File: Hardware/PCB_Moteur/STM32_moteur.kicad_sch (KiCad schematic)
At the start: 37 parts, among them J7 Conn_01x06_Pin, U5 STM32F103CBT6, Y1 830050510

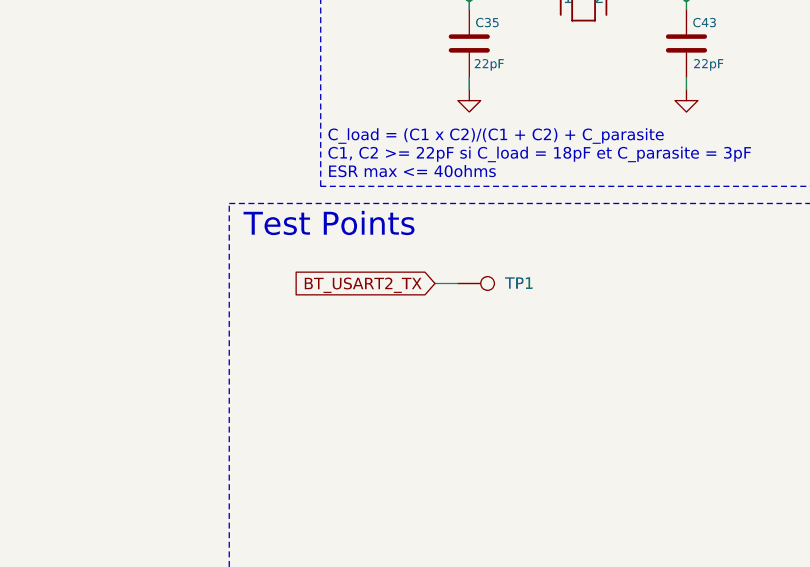
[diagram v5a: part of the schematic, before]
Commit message: fix(moteur + gse): move xt30 to border + fix silkscreen + connect shield to gnd  in pressure sensor + remake rounded corners + fix/add doc
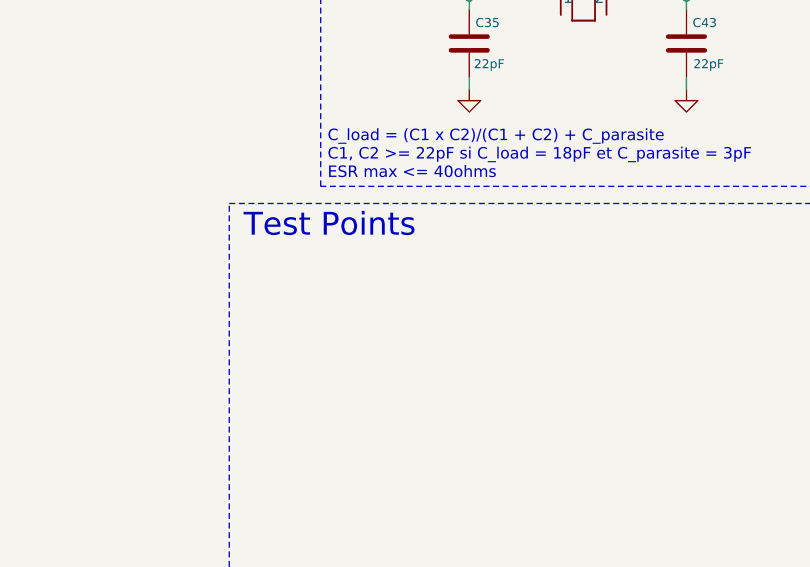
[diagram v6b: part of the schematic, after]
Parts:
- removed TP1: TestPoint, TestPoint:TestPoint_Pad_D1.0mm, symbol Connector:TestPoint
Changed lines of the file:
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@@
 	(wire
 		(pts
-			(xy 241.3 128.27) (xy 238.76 128.27)
+			(xy 242.57 105.41) (xy 242.57 106.68)
 		)
 		(stroke
@@
 	(wire
 		(pts
-			(xy 242.57 105.41) (xy 242.57 106.68)
+			(xy 146.05 44.45) (xy 146.05 46.99)
 		)
 		(stroke
@@
 	(wire
 		(pts
-			(xy 146.05 44.45) (xy 146.05 46.99)
+			(xy 215.9 25.4) (xy 218.44 25.4)
 		)
 		(stroke
@@
 	(wire
 		(pts
-			(xy 215.9 25.4) (xy 218.44 25.4)
+			(xy 148.59 127) (xy 151.13 127)
 		)
 		(stroke
@@
 	(wire
 		(pts
-			(xy 148.59 127) (xy 151.13 127)
+			(xy 132.08 82.55) (xy 133.35 82.55)
 		)
 		(stroke
@@
 	(wire
 		(pts
-			(xy 132.08 82.55) (xy 133.35 82.55)
+			(xy 166.37 67.31) (xy 173.99 67.31)
 		)
 		(stroke
@@
 	(wire
 		(pts
-			(xy 166.37 67.31) (xy 173.99 67.31)
+			(xy 132.08 102.87) (xy 133.35 102.87)
 		)
 		(stroke
@@
 		)
 	)
-	(wire
-		(pts
-			(xy 132.08 102.87) (xy 133.35 102.87)
-		)
-		(stroke
-			(width 0)
-			(type default)
-		)
-	)
 	(global_label "SYS_SWDIO"
 		(shape input)
@@
 				)
 				(justify left)
-				(hide yes)
-			)
-		)
-	)
-	(global_label "BT_USART2_TX"
-		(shape input)
-		(at 238.76 128.27 180)
-		(fields_autoplaced yes)
-		(effects
-			(font
-				(size 1.27 1.27)
-			)
-			(justify right)
-		)
-		(property "Intersheetrefs" "${INTERSHEET_REFS}"
-			(at 222.3492 128.27 0)
-			(effects
-				(font
-					(size 1.27 1.27)
-				)
-				(justify right)
 				(hide yes)
 			)
@@
 					(unit 1)
 				)
-			)
-		)
-	)
-	(symbol
-		(lib_id "Connector:TestPoint")
-		(at 241.3 128.27 270)
-		(mirror x)
-		(unit 1)
-		(exclude_from_sim no)
-		(in_bom yes)
-		(on_board yes)
-		(dnp no)
-		(property "Reference" "TP1"
-			(at 248.158 128.27 90)
-			(effects
-				(font
-					(size 1.27 1.27)
-				)
-			)
-		)
-		(property "Value" "TestPoint"
-			(at 244.602 125.73 90)
-			(effects
-				(font
-					(size 1.27 1.27)
-				)
-				(hide yes)
-			)
-		)
-		(property "Footprint" "TestPoint:TestPoint_Pad_D1.0mm"
-			(at 241.3 123.19 0)
-			(effects
-				(font
-					(size 1.27 1.27)
-				)
-				(hide yes)
-			)
-		)
-		(property "Datasheet" "-"
-			(at 241.3 123.19 0)
-			(effects
-				(font
-					(size 1.27 1.27)
-				)
-				(hide yes)
-			)
-		)
-		(property "Description" "test point"
-			(at 241.3 128.27 0)
-			(effects
-				(font
-					(size 1.27 1.27)
-				)
-				(hide yes)
-			)
-		)
-		(property "DigiKey_Part_Number" "-"
-			(at 241.3 128.27 90)
-			(effects
-				(font
-					(size 1.27 1.27)
-				)
-				(hide yes)
-			)
-		)
-		(property "Manufacturer_Part_Number" "-"
-			(at 241.3 128.27 90)
-			(effects
-				(font
-					(size 1.27 1.27)
-				)
-				(hide yes)
-			)
-		)
-		(pin "1"
-		)
-		(instances
-			(project "PCB_moteur"
-				(path "/b0d87684-7b1c-41d8-8358-755aa327573e/753d1783-c2f5-4012-bbb8-3f4eadf066f6"
-					(reference "TP1")
-					(unit 1)
-				)
-			)
-			(project "STM32_moteur"
-				(path "/da6e3e70-7434-4a0f-acc5-62316b7258e2"
-					(reference "TP?")
-					(unit 1)
-				)

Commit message: fix : BOM errors, change cutoff freq for moteur, minor fixes for GSE
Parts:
- C35, C43: DigiKey_Part_Number 1276-2891-1-ND -> 712-QSCT251Q220F1GV001ECT-ND; Manufacturer_Part_Number CL21A106KAYNNNE -> QSCT251Q220F1GV001E
- R45: DigiKey_Part_Number P1.5KDBCT-ND -> 311-1.50KCRCT-ND; Manufacturer_Part_Number ERA-3AEB152V -> RC0805FR-071K5L
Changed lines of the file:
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@@
 			)
 		)
-		(property "Datasheet" "399-C0603C103K5RACTUCT-ND"
+		(property "Datasheet" "https://www.digikey.ca/en/products/detail/kemet/C0603C103K5RACTU/411090?s=N4IgTCBcDaIMwE4EFoDCAGAbOuqCMOA0gKwBKAgqgCoCq1yAcgCIgC6AvkA"
 			(at 251.46 54.61 0)
 			(effects
@@
 			)
 		)
-		(property "Datasheet" "https://www.st.com/resource/en/datasheet/stm32f103c8.pdf"
+		(property "Datasheet" "https://www.digikey.ca/en/products/detail/stmicroelectronics/STM32F103CBT6/1754420?s=N4IgTCBcDaICwE4DsBaAbGAHJlA5AIiALoC%2BQA"
 			(at 148.59 87.63 0)
 			(effects
@@
 			)
 		)
-		(property "Datasheet" "https://www.digikey.ca/en/products/detail/samsung-electro-mechanics/CL21A106KAYNNNE/3888549"
+		(property "Datasheet" "https://www.digikey.ca/en/products/detail/johanson-technology-inc/QSCT251Q220F1GV001E/1919484"
 			(at 242.57 101.6 0)
 			(effects
@@
 			)
 		)
-		(property "DigiKey_Part_Number" "1276-2891-1-ND"
+		(property "DigiKey_Part_Number" "712-QSCT251Q220F1GV001ECT-ND"
 			(at 242.57 101.6 0)
 			(effects
@@
 			)
 		)
-		(property "Manufacturer_Part_Number" "CL21A106KAYNNNE"
+		(property "Manufacturer_Part_Number" "QSCT251Q220F1GV001E"
 			(at 242.57 101.6 0)
 			(effects
@@
 			)
 		)
-		(property "Datasheet" "https://www.digikey.ca/en/products/detail/panasonic-electronic-components/ERA-3AEB152V/1465858"
+		(property "Datasheet" "https://www.digikey.ca/en/products/detail/yageo/RC0805FR-071K5L/727496"
 			(at 212.09 25.4 0)
 			(effects
@@
 			)
 		)
-		(property "DigiKey_Part_Number" "P1.5KDBCT-ND"
+		(property "DigiKey_Part_Number" "311-1.50KCRCT-ND"
 			(at 212.09 25.4 90)
 			(effects
@@
 			)
 		)
-		(property "Manufacturer_Part_Number" "ERA-3AEB152V"
+		(property "Manufacturer_Part_Number" "RC0805FR-071K5L"
 			(at 212.09 25.4 90)
 			(effects
@@
 			)
 		)
-		(property "Datasheet" "399-C0603C103K5RACTUCT-ND"
+		(property "Datasheet" "https://www.digikey.ca/en/products/detail/kemet/C0603C103K5RACTU/411090?s=N4IgTCBcDaIMwE4EFoDCAGAbOuqCMOA0gKwBKAgqgCoCq1yAcgCIgC6AvkA"
 			(at 265.43 54.61 0)
 			(effects
@@
 			)
 		)
-		(property "Datasheet" "https://www.digikey.ca/en/products/detail/samsung-electro-mechanics/CL21A106KAYNNNE/3888549"
+		(property "Datasheet" "https://www.digikey.ca/en/products/detail/johanson-technology-inc/QSCT251Q220F1GV001E/1919484"
 			(at 266.7 101.6 0)
 			(effects
@@
 			)
 		)
-		(property "DigiKey_Part_Number" "1276-2891-1-ND"
+		(property "DigiKey_Part_Number" "712-QSCT251Q220F1GV001ECT-ND"
 			(at 266.7 101.6 0)
 			(effects
@@
 			)
 		)
-		(property "Manufacturer_Part_Number" "CL21A106KAYNNNE"
+		(property "Manufacturer_Part_Number" "QSCT251Q220F1GV001E"
 			(at 266.7 101.6 0)
 			(effects

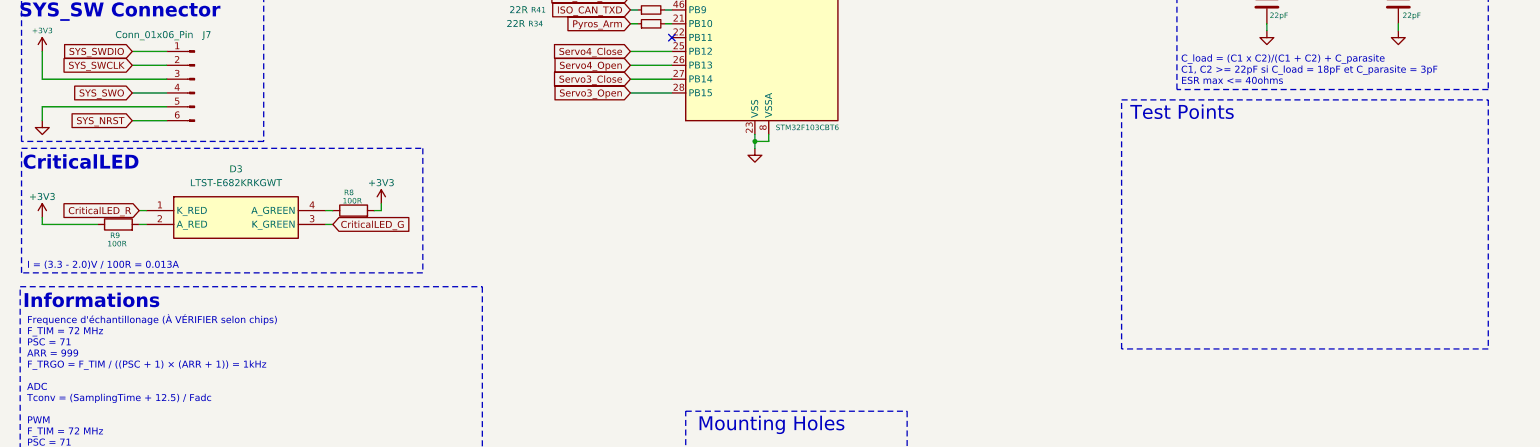
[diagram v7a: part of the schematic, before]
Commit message: fix(moteur): change Swahelok S model -> Swagelok A model (adaptable) + 100R -> 100R 1% + silkscreen
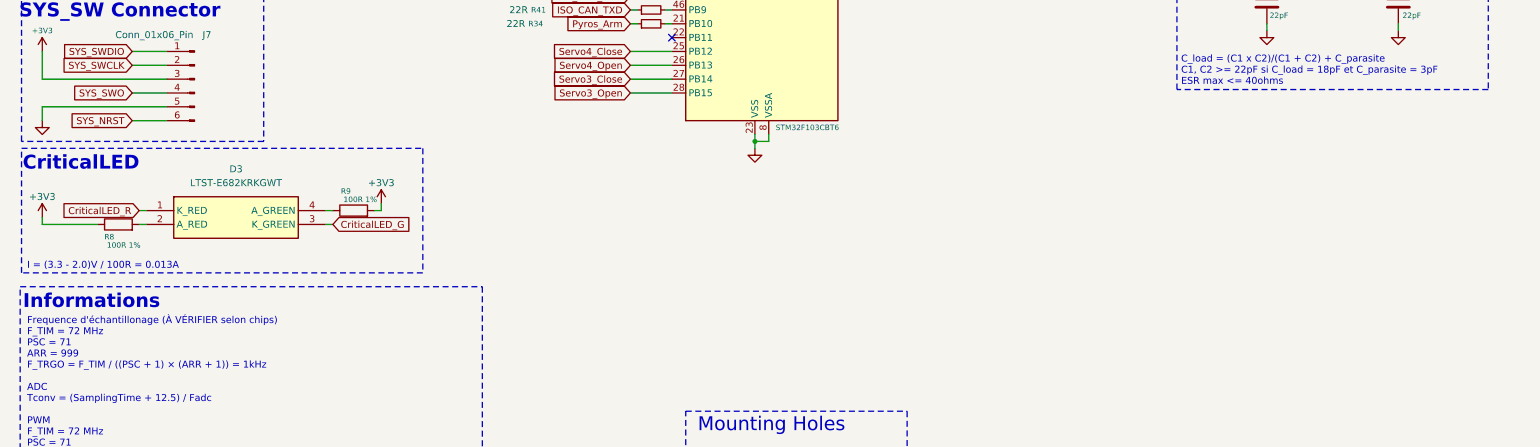
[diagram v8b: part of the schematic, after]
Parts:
- R8, R9: value 100R -> 100R 1%; DigiKey_Part_Number 541-100CCT-ND -> RT0805FRE07100RL; Manufacturer_Part_Number CRCW0805100RFKEA -> YAG3360CT-ND
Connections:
- net +3V3: now also R8.1, R9.2; no longer R8.2, R9.1
- net at D3.4 (A_GREEN): now also R9.1; no longer R8.1
- net at D3.2 (A_RED): now also R8.2; no longer R9.2
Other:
- note removed: "Test Points"
